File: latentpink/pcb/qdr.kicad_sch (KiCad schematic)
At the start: 71 parts, among them U2 XC7K160T-2FBG484C, U28 IS25WP256D-JLLE, U29 DSC1123CI2-150.0000T, U3 CY7C2245KV18-450BZXI

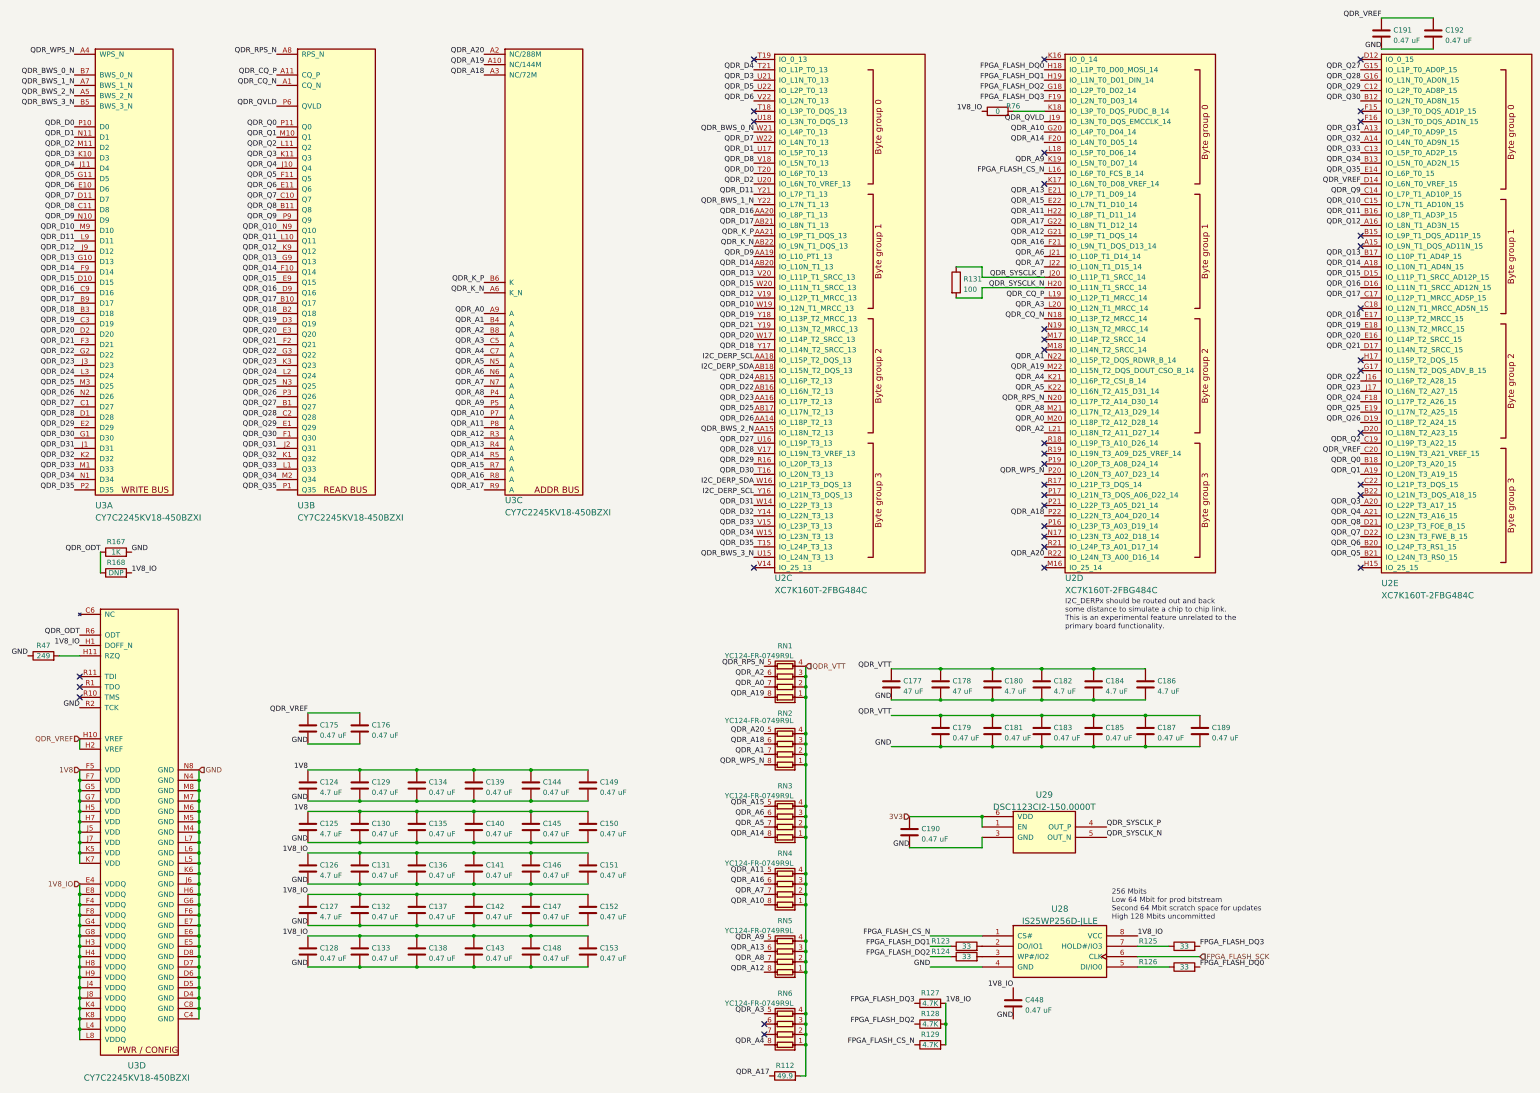
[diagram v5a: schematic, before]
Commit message: Good progress routing QDR with new pinout
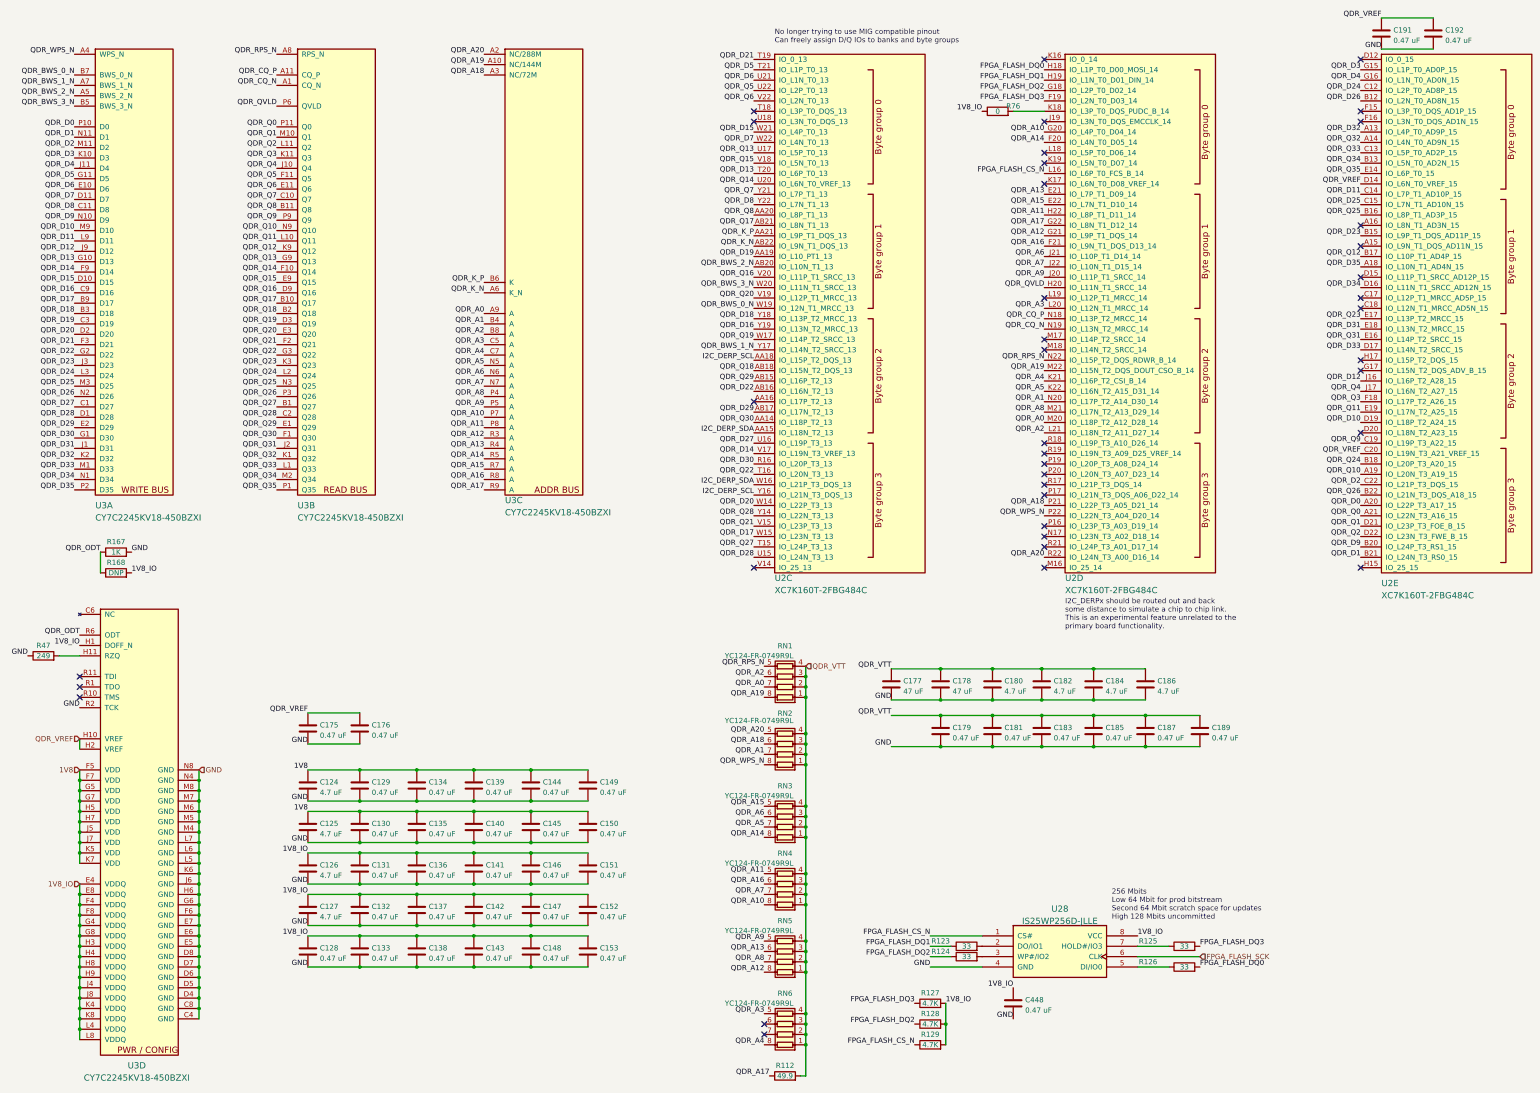
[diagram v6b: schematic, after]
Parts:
- removed C190: 0.47 uF, azonenberg_pcb:EIA_0402_CAP_NOSILK, symbol device:C
- removed R131: 100, azonenberg_pcb:EIA_0402_RES_NOSILK, symbol device:R
- removed U29: DSC1123CI2-150.0000T, azonenberg_pcb:OSCILLATOR_LVDS_3.2x2.5, symbol osc-azonenberg:OSC_LVDS_NOPAD
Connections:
- net QDR_SYSCLK_N is gone; now on net QDR_QVLD: U2.H20 (IO_L11N_T1_SRCC_14)
- net QDR_SYSCLK_P is gone; now on net QDR_A9: U2.J20 (IO_L11P_T1_SRCC_14)
- net I2C_DERP_SDA: now also U2.AA15 (IO_L18N_T2_13); no longer U2.AB18 (IO_L15N_T2_DQS_13)
- net QDR_A1: now also U2.N20 (IO_L17P_T2_A14_D30_14); no longer U2.N22 (IO_L15P_T2_DQS_RDWR_B_14)
- net QDR_A18: now also U2.P21 (IO_L22P_T3_A05_D21_14); no longer U2.P22 (IO_L22N_T3_A04_D20_14)
- net QDR_A9: no longer U2.K19 (IO_L5N_T0_D07_14)
- net QDR_BWS_0_N: now also U2.W19 (IO_12N_T1_MRCC_13); no longer U2.W21 (IO_L4P_T0_13)
- net QDR_BWS_1_N: now also U2.Y17 (IO_L14N_T2_SRCC_13); no longer U2.Y22 (IO_L7N_T1_13)
- net QDR_BWS_2_N: now also U2.AB20 (IO_L10N_T1_13); no longer U2.AA15 (IO_L18N_T2_13)
- net QDR_BWS_3_N: now also U2.W20 (IO_L11N_T1_SRCC_13); no longer U2.U15 (IO_L24N_T3_13)
- net QDR_CQ_N: now also U2.N19 (IO_L13N_T2_MRCC_14); no longer U2.N18 (IO_L13P_T2_MRCC_14)
- net QDR_CQ_P: now also U2.N18 (IO_L13P_T2_MRCC_14); no longer U2.L19 (IO_L12P_T1_MRCC_14)
- net QDR_D0: now also U2.A20 (IO_L22P_T3_A17_15); no longer U2.T20 (IO_L6P_T0_13)
- net QDR_D1: now also U2.B21 (IO_L24N_T3_RS0_15); no longer U2.U17 (IO_L5P_T0_13)
- net QDR_D10: now also U2.D19 (IO_L18P_T2_A24_15); no longer U2.W19 (IO_12N_T1_MRCC_13)
- net QDR_D11: now also U2.C14 (IO_L7P_T1_AD10P_15); no longer U2.Y21 (IO_L7P_T1_13)
- net QDR_D12: now also U2.J16 (IO_L16P_T2_A28_15); no longer U2.V19 (IO_L12P_T1_MRCC_13)
- net QDR_D13: now also U2.T20 (IO_L6P_T0_13); no longer U2.V20 (IO_L11P_T1_SRCC_13)
- net QDR_D14: now also U2.V17 (IO_L19N_T3_VREF_13); no longer U2.AB20 (IO_L10N_T1_13)
- net QDR_D15: now also U2.W21 (IO_L4P_T0_13); no longer U2.W20 (IO_L11N_T1_SRCC_13)
- net QDR_D16: now also U2.Y19 (IO_L13N_T2_MRCC_13); no longer U2.AA20 (IO_L8P_T1_13)
- net QDR_D17: now also U2.W15 (IO_L23N_T3_13); no longer U2.AB21 (IO_L8N_T1_13)
- net QDR_D18: now also U2.Y18 (IO_L13P_T2_MRCC_13); no longer U2.Y17 (IO_L14N_T2_SRCC_13)
- net QDR_D19: now also U2.AA19 (IO_L10_PT1_13); no longer U2.Y18 (IO_L13P_T2_MRCC_13)
- net QDR_D2: now also U2.C22 (IO_L21P_T3_DQS_15); no longer U2.U20 (IO_L6N_T0_VREF_13)
- net QDR_D20: now also U2.W14 (IO_L22P_T3_13); no longer U2.W17 (IO_L14P_T2_SRCC_13)
- net QDR_D21: now also U2.T19 (IO_0_13); no longer U2.Y19 (IO_L13N_T2_MRCC_13)
- net QDR_D23: now also U2.B15 (IO_L9P_T1_DQS_AD11P_15); no longer U2.AA16 (IO_L17P_T2_13)
- net QDR_D24: now also U2.C12 (IO_L2P_T0_AD8P_15); no longer U2.AB15 (IO_L16P_T2_13)
- net QDR_D25: now also U2.C15 (IO_L7N_T1_AD10N_15); no longer U2.AB17 (IO_L17N_T2_13)
- net QDR_D26: now also U2.B12 (IO_L2N_T0_AD8N_15); no longer U2.AA14 (IO_L18P_T2_13)
- net QDR_D28: now also U2.U15 (IO_L24N_T3_13); no longer U2.V17 (IO_L19N_T3_VREF_13)
- net QDR_D29: now also U2.AB17 (IO_L17N_T2_13); no longer U2.R16 (IO_L20P_T3_13)
- net QDR_D3: now also U2.G15 (IO_L1P_T0_AD0P_15); no longer U2.U21 (IO_L1N_T0_13)
- net QDR_D30: now also U2.R16 (IO_L20P_T3_13); no longer U2.T16 (IO_L20N_T3_13)
- net QDR_D31: now also U2.E18 (IO_L13N_T2_MRCC_15); no longer U2.W14 (IO_L22P_T3_13)
- net QDR_D32: now also U2.A13 (IO_L4P_T0_AD9P_15); no longer U2.Y14 (IO_L22N_T3_13)
- net QDR_D33: now also U2.D17 (IO_L14N_T2_SRCC_15); no longer U2.V15 (IO_L23P_T3_13)
- net QDR_D34: now also U2.D16 (IO_L11N_T1_SRCC_AD12N_15); no longer U2.W15 (IO_L23N_T3_13)
- net QDR_D35: now also U2.A18 (IO_L10N_T1_AD4N_15); no longer U2.T15 (IO_L24P_T3_13)
- net QDR_D4: now also U2.G16 (IO_L1N_T0_AD0N_15); no longer U2.T21 (IO_L1P_T0_13)
- net QDR_D5: now also U2.T21 (IO_L1P_T0_13); no longer U2.U22 (IO_L2P_T0_13)
- net QDR_D6: now also U2.U21 (IO_L1N_T0_13); no longer U2.V22 (IO_L2N_T0_13)
- net QDR_D8: now also U2.Y22 (IO_L7N_T1_13); no longer U2.V18 (IO_L5N_T0_13)
- net QDR_D9: now also U2.B20 (IO_L24P_T3_RS1_15); no longer U2.AA19 (IO_L10_PT1_13)
- net QDR_Q0: now also U2.A21 (IO_L22N_T3_A16_15); no longer U2.B18 (IO_L20P_T3_A20_15)
- net QDR_Q1: now also U2.D21 (IO_L23P_T3_FOE_B_15); no longer U2.A19 (IO_L20N_T3_A19_15)
- net QDR_Q10: now also U2.A19 (IO_L20N_T3_A19_15); no longer U2.C15 (IO_L7N_T1_AD10N_15)
- net QDR_Q11: now also U2.E19 (IO_L17N_T2_A25_15); no longer U2.B16 (IO_L8P_T1_AD3P_15)
- net QDR_Q12: now also U2.B17 (IO_L10P_T1_AD4P_15); no longer U2.A16 (IO_L8N_T1_AD3N_15)
- net QDR_Q13: now also U2.U17 (IO_L5P_T0_13); no longer U2.B17 (IO_L10P_T1_AD4P_15)
- net QDR_Q14: now also U2.U20 (IO_L6N_T0_VREF_13); no longer U2.A18 (IO_L10N_T1_AD4N_15)
- net QDR_Q15: now also U2.V18 (IO_L5N_T0_13); no longer U2.D15 (IO_L11P_T1_SRCC_AD12P_15)
- net QDR_Q16: now also U2.V20 (IO_L11P_T1_SRCC_13); no longer U2.D16 (IO_L11N_T1_SRCC_AD12N_15)
- net QDR_Q17: now also U2.AB21 (IO_L8N_T1_13); no longer U2.C17 (IO_L12P_T1_MRCC_AD5P_15)
- net QDR_Q18: now also U2.AB18 (IO_L15N_T2_DQS_13); no longer U2.E17 (IO_L13P_T2_MRCC_15)
- net QDR_Q19: now also U2.W17 (IO_L14P_T2_SRCC_13); no longer U2.E18 (IO_L13N_T2_MRCC_15)
- net QDR_Q2: now also U2.D22 (IO_L23N_T3_FWE_B_15); no longer U2.C19 (IO_L19P_T3_A22_15)
- net QDR_Q20: now also U2.V19 (IO_L12P_T1_MRCC_13); no longer U2.E16 (IO_L14P_T2_SRCC_15)
- net QDR_Q21: now also U2.V15 (IO_L23P_T3_13); no longer U2.D17 (IO_L14N_T2_SRCC_15)
- net QDR_Q22: now also U2.T16 (IO_L20N_T3_13); no longer U2.J16 (IO_L16P_T2_A28_15)
- net QDR_Q23: now also U2.E17 (IO_L13P_T2_MRCC_15); no longer U2.J17 (IO_L16N_T2_A27_15)
- net QDR_Q24: now also U2.B18 (IO_L20P_T3_A20_15); no longer U2.F18 (IO_L17P_T2_A26_15)
- net QDR_Q25: now also U2.B16 (IO_L8P_T1_AD3P_15); no longer U2.E19 (IO_L17N_T2_A25_15)
- net QDR_Q26: now also U2.B22 (IO_L21N_T3_DQS_A18_15); no longer U2.D19 (IO_L18P_T2_A24_15)
- net QDR_Q27: now also U2.T15 (IO_L24P_T3_13); no longer U2.G15 (IO_L1P_T0_AD0P_15)
- net QDR_Q28: now also U2.Y14 (IO_L22N_T3_13); no longer U2.G16 (IO_L1N_T0_AD0N_15)
- net QDR_Q29: now also U2.AB15 (IO_L16P_T2_13); no longer U2.C12 (IO_L2P_T0_AD8P_15)
- net QDR_Q3: now also U2.F18 (IO_L17P_T2_A26_15); no longer U2.A20 (IO_L22P_T3_A17_15)
- net QDR_Q30: now also U2.AA14 (IO_L18P_T2_13); no longer U2.B12 (IO_L2N_T0_AD8N_15)
- net QDR_Q31: now also U2.E16 (IO_L14P_T2_SRCC_15); no longer U2.A13 (IO_L4P_T0_AD9P_15)
- net QDR_Q4: now also U2.J17 (IO_L16N_T2_A27_15); no longer U2.A21 (IO_L22N_T3_A16_15)
- net QDR_Q5: now also U2.U22 (IO_L2P_T0_13); no longer U2.B21 (IO_L24N_T3_RS0_15)
- net QDR_Q6: now also U2.V22 (IO_L2N_T0_13); no longer U2.B20 (IO_L24P_T3_RS1_15)
- net QDR_Q7: now also U2.Y21 (IO_L7P_T1_13); no longer U2.D22 (IO_L23N_T3_FWE_B_15)
- net QDR_Q8: now also U2.AA20 (IO_L8P_T1_13); no longer U2.D21 (IO_L23P_T3_FOE_B_15)
- net QDR_Q9: now also U2.C19 (IO_L19P_T3_A22_15); no longer U2.C14 (IO_L7P_T1_AD10P_15)
- net QDR_QVLD: no longer U2.J19 (IO_L3N_T0_DQS_EMCCLK_14)
- net QDR_RPS_N: now also U2.N22 (IO_L15P_T2_DQS_RDWR_B_14); no longer U2.N20 (IO_L17P_T2_A14_D30_14)
- net QDR_WPS_N: now also U2.P22 (IO_L22N_T3_A04_D20_14); no longer U2.P20 (IO_L20N_T3_A07_D23_14)
- no-connect marks 37 -> 39
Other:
- note added: "No longer trying to use MIG compatible pinout Can freely assign D/Q IOs to banks and byte groups"
